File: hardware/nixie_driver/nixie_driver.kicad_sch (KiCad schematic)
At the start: 44 parts, among them J5 Conn_01x03, J6 Conn_01x03, J7 Conn_02x03_Odd_Even, U8 CD40109B, U9 TubeClock_HV5622

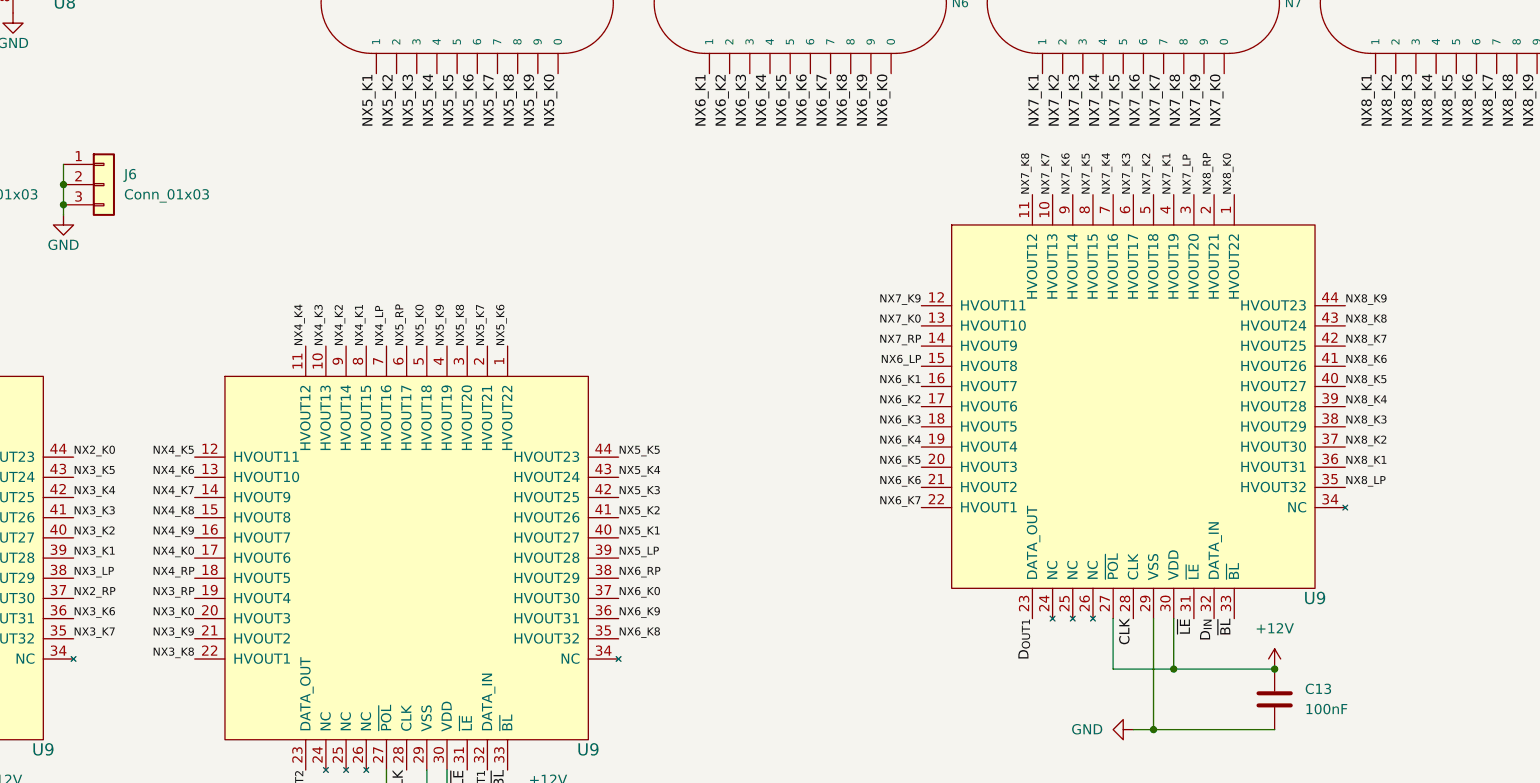
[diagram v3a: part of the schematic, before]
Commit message: Finish PCB design for nixie_driver
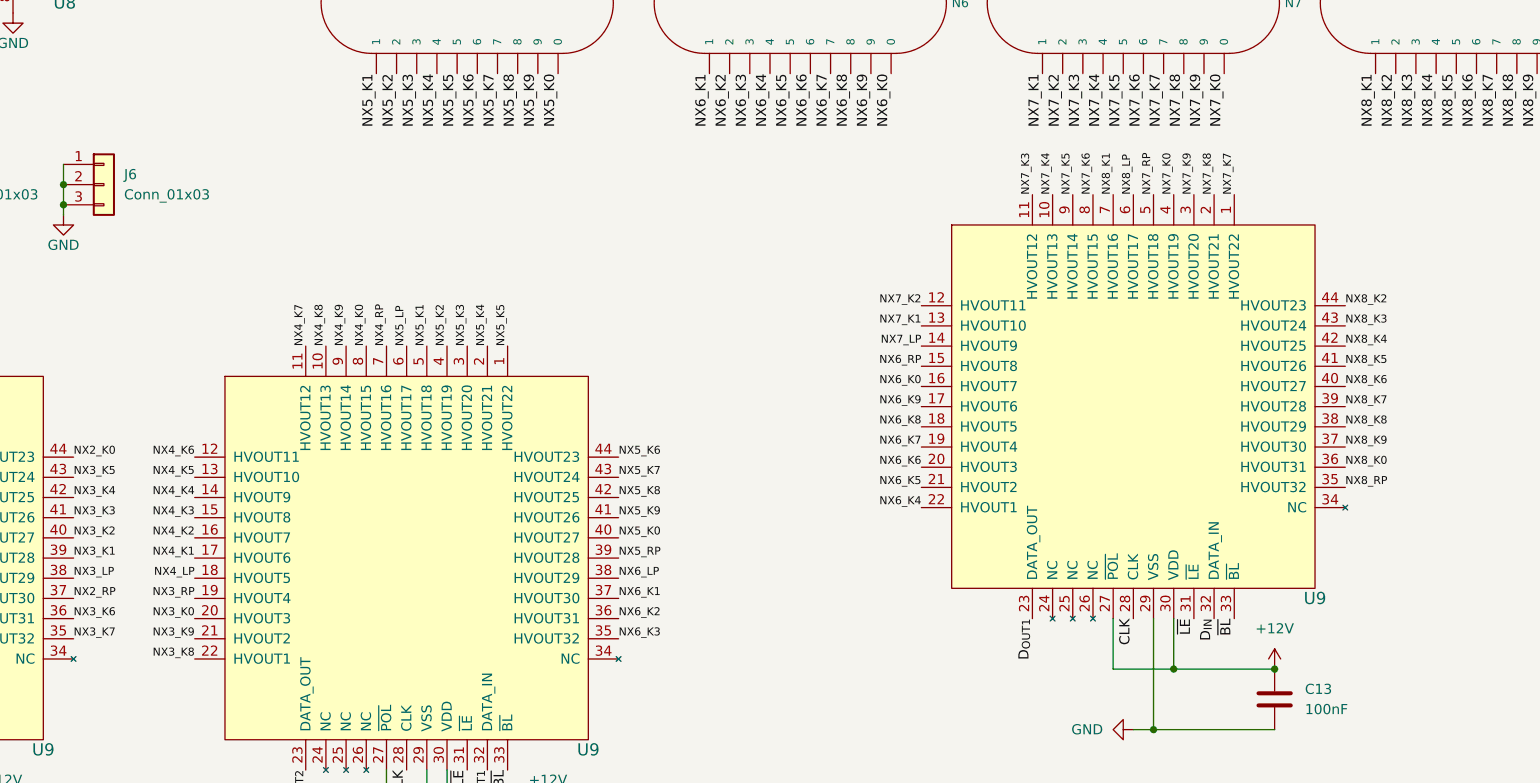
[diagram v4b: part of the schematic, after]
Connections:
- net NX4_K0: now also U9.8 (HVOUT15); no longer U9.17 (HVOUT6)
- net NX4_K1: now also U9.17 (HVOUT6); no longer U9.8 (HVOUT15)
- net NX4_K2: now also U9.16 (HVOUT7); no longer U9.9 (HVOUT14)
- net NX4_K3: now also U9.15 (HVOUT8); no longer U9.10 (HVOUT13)
- net NX4_K4: now also U9.14 (HVOUT9); no longer U9.11 (HVOUT12)
- net NX4_K5: now also U9.13 (HVOUT10); no longer U9.12 (HVOUT11)
- net NX4_K6: now also U9.12 (HVOUT11); no longer U9.13 (HVOUT10)
- net NX4_K7: now also U9.11 (HVOUT12); no longer U9.14 (HVOUT9)
- net NX4_K8: now also U9.10 (HVOUT13); no longer U9.15 (HVOUT8)
- net NX4_K9: now also U9.9 (HVOUT14); no longer U9.16 (HVOUT7)
- net NX4_LP: now also U9.18 (HVOUT5); no longer U9.7 (HVOUT16)
- net NX4_RP: now also U9.7 (HVOUT16); no longer U9.18 (HVOUT5)
- net NX5_K0: now also U9.40 (HVOUT27); no longer U9.5 (HVOUT18)
- net NX5_K1: now also U9.5 (HVOUT18); no longer U9.40 (HVOUT27)
- net NX5_K2: now also U9.4 (HVOUT19); no longer U9.41 (HVOUT26)
- net NX5_K3: now also U9.3 (HVOUT20); no longer U9.42 (HVOUT25)
- net NX5_K4: now also U9.2 (HVOUT21); no longer U9.43 (HVOUT24)
- net NX5_K5: now also U9.1 (HVOUT22); no longer U9.44 (HVOUT23)
- net NX5_K6: now also U9.44 (HVOUT23); no longer U9.1 (HVOUT22)
- net NX5_K7: now also U9.43 (HVOUT24); no longer U9.2 (HVOUT21)
- net NX5_K8: now also U9.42 (HVOUT25); no longer U9.3 (HVOUT20)
- net NX5_K9: now also U9.41 (HVOUT26); no longer U9.4 (HVOUT19)
- net NX5_LP: now also U9.6 (HVOUT17); no longer U9.39 (HVOUT28)
- net NX5_RP: now also U9.39 (HVOUT28); no longer U9.6 (HVOUT17)
- net NX6_K0: now also U9.16 (HVOUT7); no longer U9.37 (HVOUT30)
- net NX6_K1: now also U9.37 (HVOUT30); no longer U9.16 (HVOUT7)
- net NX6_K2: now also U9.36 (HVOUT31); no longer U9.17 (HVOUT6)
- net NX6_K3: now also U9.35 (HVOUT32); no longer U9.18 (HVOUT5)
- net NX6_K4: now also U9.22 (HVOUT1); no longer U9.19 (HVOUT4)
- net NX6_K5: now also U9.21 (HVOUT2); no longer U9.20 (HVOUT3)
- net NX6_K6: now also U9.20 (HVOUT3); no longer U9.21 (HVOUT2)
- net NX6_K7: now also U9.19 (HVOUT4); no longer U9.22 (HVOUT1)
- net NX6_K8: now also U9.18 (HVOUT5); no longer U9.35 (HVOUT32)
- net NX6_K9: now also U9.17 (HVOUT6); no longer U9.36 (HVOUT31)
- net NX6_LP: now also U9.38 (HVOUT29); no longer U9.15 (HVOUT8)
- net NX6_RP: now also U9.15 (HVOUT8); no longer U9.38 (HVOUT29)
- net NX7_K0: now also U9.4 (HVOUT19); no longer U9.13 (HVOUT10)
- net NX7_K1: now also U9.13 (HVOUT10); no longer U9.4 (HVOUT19)
- net NX7_K2: now also U9.12 (HVOUT11); no longer U9.5 (HVOUT18)
- net NX7_K3: now also U9.11 (HVOUT12); no longer U9.6 (HVOUT17)
- net NX7_K4: now also U9.10 (HVOUT13); no longer U9.7 (HVOUT16)
- net NX7_K5: now also U9.9 (HVOUT14); no longer U9.8 (HVOUT15)
- net NX7_K6: now also U9.8 (HVOUT15); no longer U9.9 (HVOUT14)
- net NX7_K7: now also U9.1 (HVOUT22); no longer U9.10 (HVOUT13)
- net NX7_K8: now also U9.2 (HVOUT21); no longer U9.11 (HVOUT12)
- net NX7_K9: now also U9.3 (HVOUT20); no longer U9.12 (HVOUT11)
- net NX7_LP: now also U9.14 (HVOUT9); no longer U9.3 (HVOUT20)
- net NX7_RP: now also U9.5 (HVOUT18); no longer U9.14 (HVOUT9)
- net NX8_K0: now also U9.36 (HVOUT31); no longer U9.1 (HVOUT22)
- net NX8_K1: now also U9.7 (HVOUT16); no longer U9.36 (HVOUT31)
- net NX8_K2: now also U9.44 (HVOUT23); no longer U9.37 (HVOUT30)
- net NX8_K3: now also U9.43 (HVOUT24); no longer U9.38 (HVOUT29)
- net NX8_K4: now also U9.42 (HVOUT25); no longer U9.39 (HVOUT28)
- net NX8_K5: now also U9.41 (HVOUT26); no longer U9.40 (HVOUT27)
- net NX8_K6: now also U9.40 (HVOUT27); no longer U9.41 (HVOUT26)
- net NX8_K7: now also U9.39 (HVOUT28); no longer U9.42 (HVOUT25)
- net NX8_K8: now also U9.38 (HVOUT29); no longer U9.43 (HVOUT24)
- net NX8_K9: now also U9.37 (HVOUT30); no longer U9.44 (HVOUT23)
- net NX8_LP: now also U9.6 (HVOUT17); no longer U9.35 (HVOUT32)
- net NX8_RP: now also U9.35 (HVOUT32); no longer U9.2 (HVOUT21)
